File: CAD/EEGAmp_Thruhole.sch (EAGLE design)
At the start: 14 parts, among them U1 TL084BCN

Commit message: corrected notes
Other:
- note added: "VREF can be VDD or a dedicated ADC voltage reference"
- note removed: "VRef can be a voltage divider circuit if on battery power"
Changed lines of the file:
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@@
 R7: 1kΩ
 R8: 1MΩ</text>
-<text x="218.44" y="86.36" size="1.778" layer="97">VRef can be a voltage divider
-circuit if on battery power</text>
+<text x="218.44" y="86.36" size="1.778" layer="97">VREF can be VDD or a dedicated
+ADC voltage reference</text>
 </plain>
 <instances>

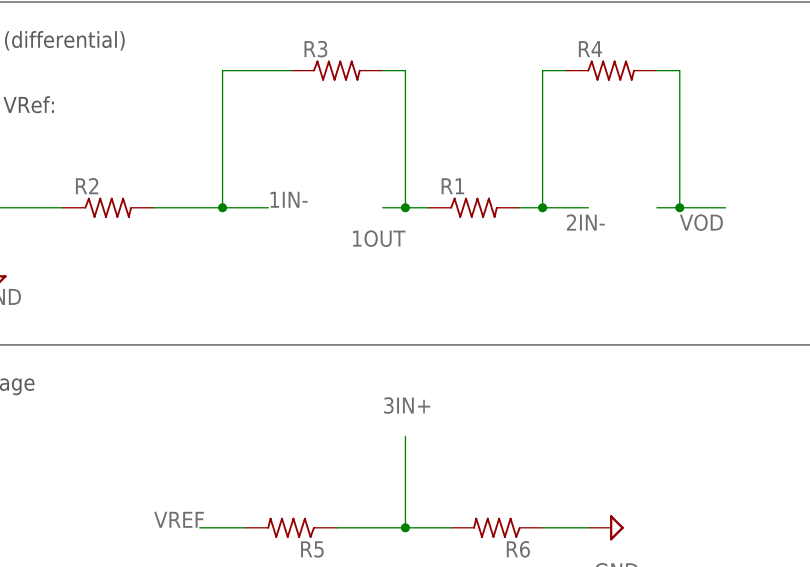
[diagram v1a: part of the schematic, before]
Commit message: added a filter cap on inputs
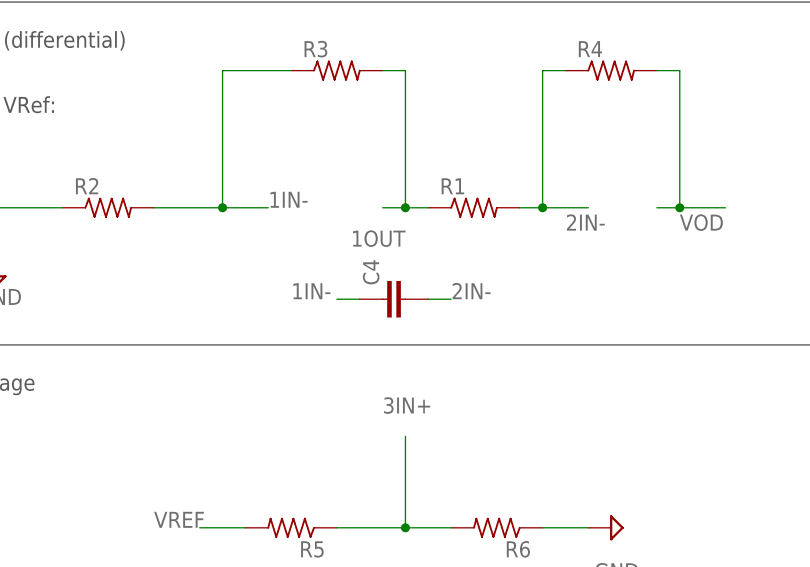
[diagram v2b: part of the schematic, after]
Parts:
- added C4: (no value), capacitor-wima:C2.5/2
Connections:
- net 1IN-: now also C4.1
- net 2IN-: now also C4.2
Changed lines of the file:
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@@
 <part name="JP2" library="pinhead" library_urn="urn:adsk.eagle:library:325" deviceset="PINHD-1X4" device="" package3d_urn="urn:adsk.eagle:package:22407/2"/>
 <part name="JP1" library="pinhead" library_urn="urn:adsk.eagle:library:325" deviceset="PINHD-1X3" device="" package3d_urn="urn:adsk.eagle:package:22458/2"/>
+<part name="C4" library="capacitor-wima" library_urn="urn:adsk.eagle:library:116" deviceset="C" device="2.5/2" package3d_urn="urn:adsk.eagle:package:5415/1"/>
 </parts>
 <sheets>
@@
 <attribute name="VALUE" x="148.59" y="35.56" size="1.778" layer="96" rot="R180"/>
 </instance>
+<instance part="C4" gate="G$1" x="78.74" y="83.82" smashed="yes" rot="R90">
+<attribute name="NAME" x="78.359" y="85.344" size="1.778" layer="95" rot="R90"/>
+<attribute name="VALUE" x="83.439" y="85.344" size="1.778" layer="96" rot="R90"/>
+</instance>
 </instances>
 <busses>
@@
 <junction x="96.52" y="93.98"/>
 <label x="99.06" y="91.44" size="1.778" layer="95"/>
+</segment>
+<segment>
+<pinref part="C4" gate="G$1" pin="2"/>
+<wire x1="83.82" y1="83.82" x2="86.36" y2="83.82" width="0.1524" layer="91"/>
+<label x="86.36" y="83.82" size="1.778" layer="95"/>
 </segment>
 </net>
@@
 <junction x="60.96" y="93.98"/>
 </segment>
-</net>
+<segment>
+<pinref part="C4" gate="G$1" pin="1"/>
+<wire x1="76.2" y1="83.82" x2="73.66" y2="83.82" width="0.1524" layer="91"/>
+<label x="68.58" y="83.82" size="1.778" layer="95"/>
+</segment>
+</net>
